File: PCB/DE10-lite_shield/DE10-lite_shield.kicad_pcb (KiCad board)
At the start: 2 copper layers, 4 parts

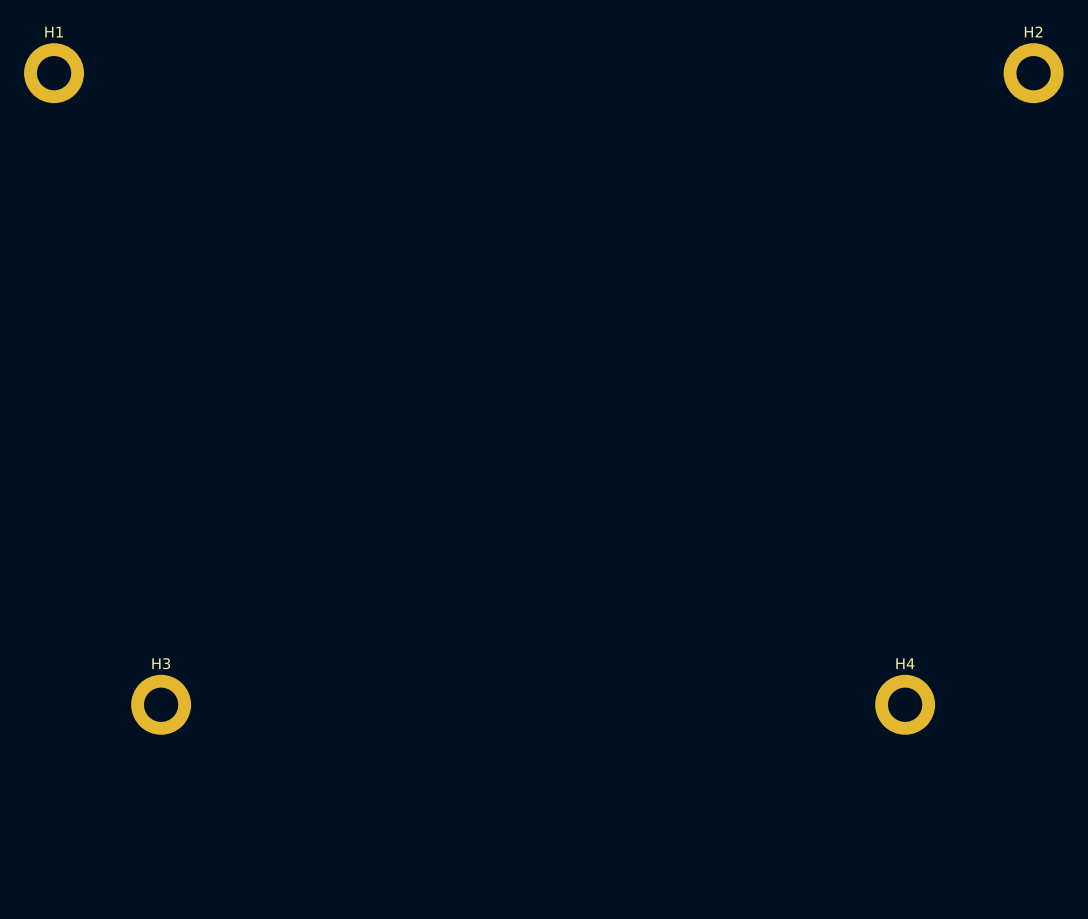
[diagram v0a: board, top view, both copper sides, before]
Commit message: Updated PCB dimensions
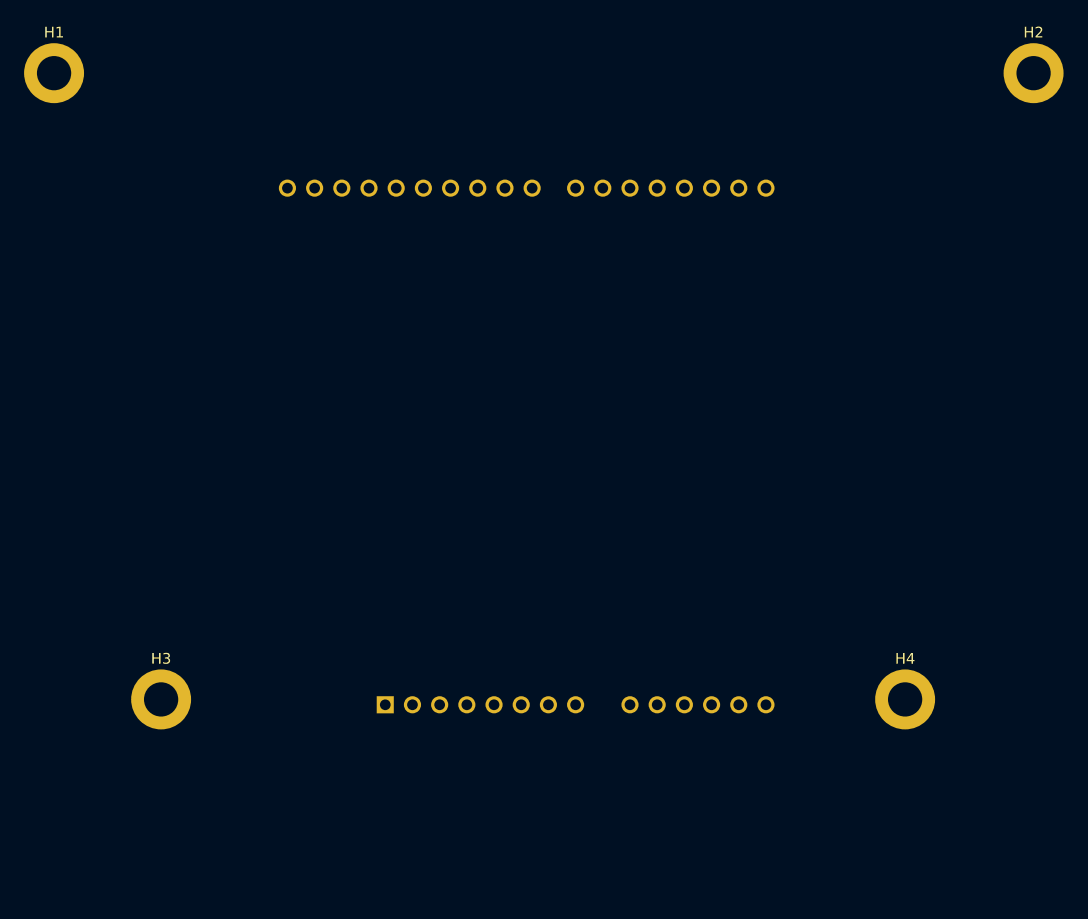
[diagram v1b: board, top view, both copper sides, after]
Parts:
- added A1: UNO_R3_SHIELD, footprints:UNO_R3_SHIELD, B.Cu at (133.9, 112.0)
- moved H3 0.50 mm to (113.0, 111.5)
- moved H4 0.50 mm to (182.5, 111.5)

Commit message: Created 3D model
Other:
- board outline added: 97.5 x 80 mm
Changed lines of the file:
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@@
   (gr_rect (start 100 50) (end 197.5 130)
     (stroke (width 0.15) (type default)) (fill none) (layer "Dwgs.User"))
+  (gr_rect (start 100 106) (end 106 111)
+    (stroke (width 0.1) (type default)) (fill none) (layer "Dwgs.User"))
   (gr_rect (start 182.5 111.5) (end 197.5 130)
     (stroke (width 0.15) (type default)) (fill none) (layer "Dwgs.User"))
@@
   (gr_rect (start 194.5 57.5) (end 197.5 88.5)
     (stroke (width 0.15) (type default)) (fill none) (layer "Dwgs.User"))
+  (gr_line (start 197.5 130) (end 197.5 89)
+    (stroke (width 0.1) (type default)) (layer "Edge.Cuts"))
+  (gr_line (start 100 105.5) (end 106.5 105.5)
+    (stroke (width 0.1) (type default)) (layer "Edge.Cuts"))
+  (gr_line (start 179 50) (end 179 59.5)
+    (stroke (width 0.1) (type default)) (layer "Edge.Cuts"))
+  (gr_line (start 197.5 89) (end 194 89)
+    (stroke (width 0.1) (type default)) (layer "Edge.Cuts"))
+  (gr_line (start 100 50) (end 100 105.5)
+    (stroke (width 0.1) (type default)) (layer "Edge.Cuts"))
+  (gr_line (start 197.5 50) (end 179 50)
+    (stroke (width 0.1) (type default)) (layer "Edge.Cuts"))
+  (gr_line (start 118.5 50) (end 100 50)
+    (stroke (width 0.1) (type default)) (layer "Edge.Cuts"))
+  (gr_line (start 194 57) (end 197.5 57)
+    (stroke (width 0.1) (type default)) (layer "Edge.Cuts"))
+  (gr_line (start 100 130) (end 197.5 130)
+    (stroke (width 0.1) (type default)) (layer "Edge.Cuts"))
+  (gr_line (start 118.5 59.5) (end 118.5 50)
+    (stroke (width 0.1) (type default)) (layer "Edge.Cuts"))
+  (gr_line (start 194 89) (end 194 57)
+    (stroke (width 0.1) (type default)) (layer "Edge.Cuts"))
+  (gr_line (start 179 59.5) (end 118.5 59.5)
+    (stroke (width 0.1) (type default)) (layer "Edge.Cuts"))
+  (gr_line (start 100 111.5) (end 100 130)
+    (stroke (width 0.1) (type default)) (layer "Edge.Cuts"))
+  (gr_line (start 106.5 111.5) (end 100 111.5)
+    (stroke (width 0.1) (type default)) (layer "Edge.Cuts"))
+  (gr_line (start 197.5 57) (end 197.5 50)
+    (stroke (width 0.1) (type default)) (layer "Edge.Cuts"))
+  (gr_line (start 106.5 105.5) (end 106.5 111.5)
+    (stroke (width 0.1) (type default)) (layer "Edge.Cuts"))
   (dimension (type aligned) (layer "Cmts.User")
     (pts (xy 97 80) (xy 114 80))
@@
   )
   (dimension (type aligned) (layer "Cmts.User")
-    (pts (xy 113 111.5) (xy 100 111.5))
-    (height 5.999999)
-    (gr_text "13.0000 mm" (at 106.5 104.350001) (layer "Cmts.User")
+    (pts (xy 100 106) (xy 106 106))
+    (height -3.5)
+    (gr_text "6.0000 mm" (at 103 101.35) (layer "Cmts.User")
       (effects (font (size 1 1) (thickness 0.15)))
     )
     (format (prefix "") (suffix "") (units 3) (units_format 1) (precision 4))
     (style (thickness 0.15) (arrow_length 1.27) (text_position_mode 0) (extension_height 0.58642) (extension_offset 0.5) keep_text_aligned)
+  )
+  (dimension (type aligned) (layer "Cmts.User")
+    (pts (xy 113 111.5) (xy 100 111.5))
+    (height 5.999999)
+    (gr_text "13.0000 mm" (at 106.5 104.5) (layer "Cmts.User")
+      (effects (font (size 1 1) (thickness 0.15)))
+    )
+    (format (prefix "") (suffix "") (units 3) (units_format 1) (precision 4))
+    (style (thickness 0.15) (arrow_length 1.27) (text_position_mode 2) (extension_height 0.58642) (extension_offset 0.5) keep_text_aligned)
   )
   (dimension (type aligned) (layer "Cmts.User")
@@
   )
   (dimension (type aligned) (layer "Cmts.User")
+    (pts (xy 100 111) (xy 100 106))
+    (height -5)
+    (gr_text "5.0000 mm" (at 93.85 108.5 90) (layer "Cmts.User")
+      (effects (font (size 1 1) (thickness 0.15)))
+    )
+    (format (prefix "") (suffix "") (units 3) (units_format 1) (precision 4))
+    (style (thickness 0.15) (arrow_length 1.27) (text_position_mode 0) (extension_height 0.58642) (extension_offset 0.5) keep_text_aligned)
+  )
+  (dimension (type aligned) (layer "Cmts.User")
     (pts (xy 197.5 112) (xy 169.5 112))
     (height 9.499999)
@@
   )
   (dimension (type aligned) (layer "Cmts.User")
-    (pts (xy 100 50) (xy 100 130))
+    (pts (xy 96.999999 50) (xy 96.999999 130))
     (height 4.999999)
-    (gr_text "80.0000 mm" (at 93.850001 90 90) (layer "Cmts.User")
+    (gr_text "80.0000 mm" (at 90.85 90 90) (layer "Cmts.User")
       (effects (font (size 1 1) (thickness 0.15)))
     )
@@
       (effects (font (size 1 1) (thickness 0.15)))
     )
+    (format (prefix "") (suffix "") (units 3) (units_format 1) (precision 4))
+    (style (thickness 0.15) (arrow_length 1.27) (text_position_mode 0) (extension_height 0.58642) (extension_offset 0.5) keep_text_aligned)
+  )
+  (dimension (type aligned) (layer "Cmts.User")
+    (pts (xy 100 130) (xy 100 111))
+    (height -5)
+    (gr_text "19.0000 mm" (at 93.85 120.5 90) (layer "Cmts.User")
+      (effects (font (size 1 1) (thickness 0.15)))
+    )
